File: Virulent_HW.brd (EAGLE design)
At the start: 58.2 x 43 mm, 102 parts, among them SW1 COM08229, SW2 COM08720, SW3 BUTTON, U1 STM32F050G6U6, U2 MAX14536, X1 SMA-142-0711-821/826

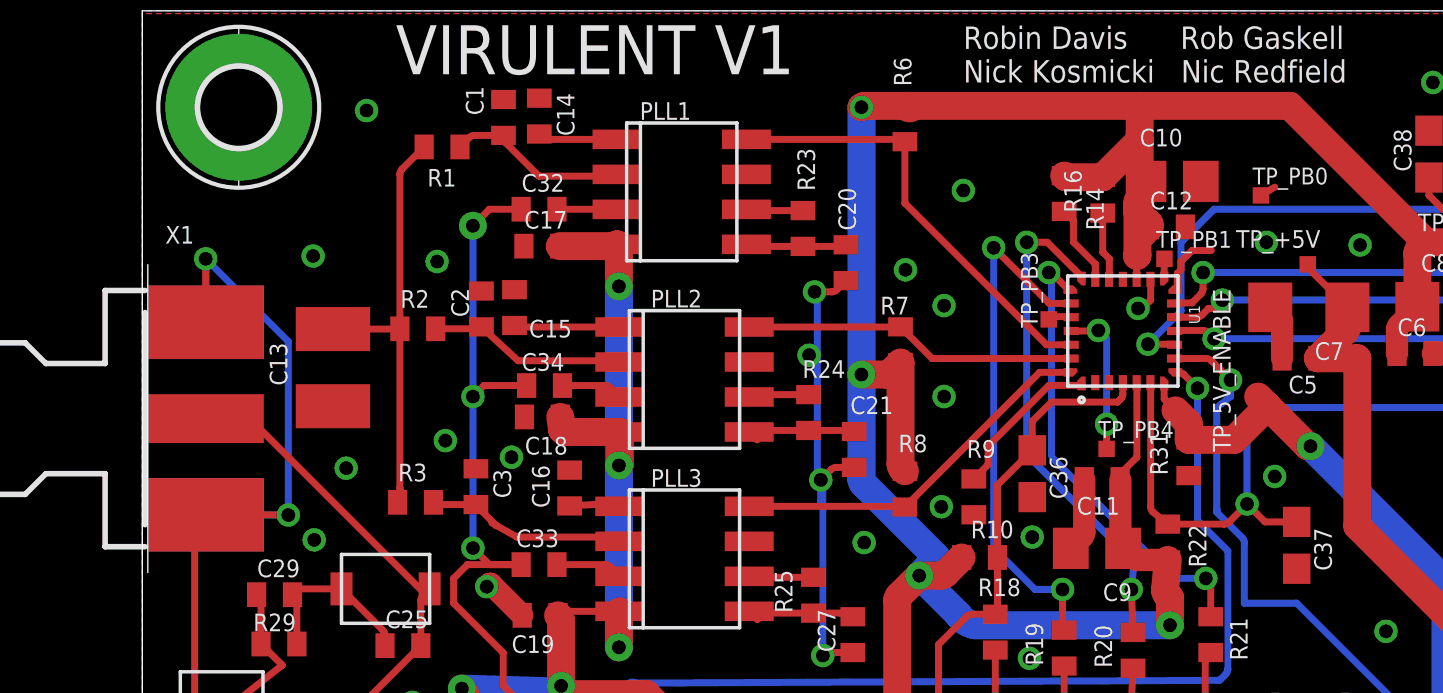
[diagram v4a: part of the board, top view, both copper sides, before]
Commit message: modified silkscreen
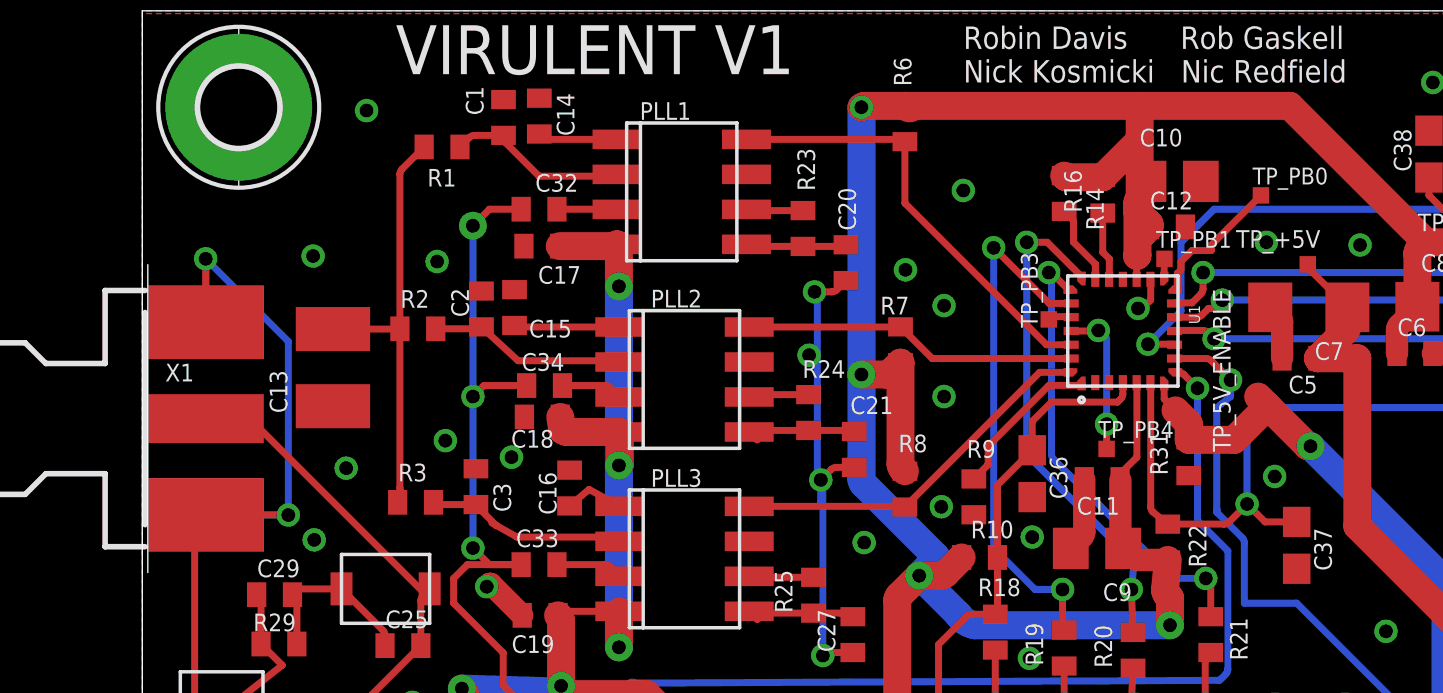
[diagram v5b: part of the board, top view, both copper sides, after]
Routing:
- net PB0: track 2.92 -> 5.09 mm
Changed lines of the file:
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@@
 <setting verticaltext="up"/>
 </settings>
-<grid distance="0.5" unitdist="mm" unit="mm" style="dots" multiple="1" display="no" altdistance="0.05" altunitdist="mm" altunit="mm"/>
+<grid distance="0.5" unitdist="mm" unit="mm" style="dots" multiple="1" display="no" altdistance="0.25" altunitdist="mm" altunit="mm"/>
 <layers>
 <layer number="1" name="Top" color="4" fill="1" visible="yes" active="yes"/>
-<layer number="16" name="Bottom" color="1" fill="1" visible="yes" active="yes"/>
+<layer number="16" name="Bottom" color="1" fill="1" visible="no" active="yes"/>
 <layer number="17" name="Pads" color="2" fill="1" visible="yes" active="yes"/>
 <layer number="18" name="Vias" color="2" fill="1" visible="yes" active="yes"/>
@@
 </element>
 <element name="C3" library="rcl" package="C0402" value="0.1u" x="12.11" y="25.73" smashed="yes" rot="R270">
-<attribute name="NAME" x="12.745" y="26.365" size="0.64" layer="25" rot="R270"/>
+<attribute name="NAME" x="12.745" y="25.865" size="0.64" layer="25" rot="R270"/>
 </element>
 <element name="R3" library="Virulent_HW" package="R0402" value="4.7k" x="9.92" y="25.16" smashed="yes">
@@
 </element>
 <element name="C16" library="rcl" package="C0402" value="2.2u" x="15.51" y="25.68" smashed="yes" rot="R270">
-<attribute name="NAME" x="14.145" y="26.515" size="0.64" layer="25" rot="R270"/>
+<attribute name="NAME" x="14.395" y="26.265" size="0.64" layer="25" rot="R270"/>
 </element>
 <element name="C17" library="rcl" package="C0402" value="1n" x="14.5" y="34.46" smashed="yes">
-<attribute name="NAME" x="13.865" y="35.095" size="0.64" layer="25"/>
+<attribute name="NAME" x="14.365" y="33.095" size="0.64" layer="25"/>
 </element>
 <element name="C18" library="rcl" package="C0402" value="1n" x="14.52" y="28.26" smashed="yes">
-<attribute name="NAME" x="13.885" y="26.895" size="0.64" layer="25"/>
+<attribute name="NAME" x="13.385" y="27.145" size="0.64" layer="25"/>
 </element>
 <element name="C19" library="rcl" package="C0402" value="1n" x="14.44" y="21.06" smashed="yes">
@@
 </element>
 <element name="C13" library="rcl" package="C1210" value="250u" x="6.92" y="30.05" smashed="yes" rot="R270">
-<attribute name="NAME" x="4.625" y="30.955" size="0.64" layer="25" rot="R270"/>
+<attribute name="NAME" x="4.625" y="29.955" size="0.64" layer="25" rot="R270"/>
 </element>
 <element name="R31" library="Virulent_HW" package="R0402" value="10k" x="37.98" y="26.78" smashed="yes" rot="R90">
@@
 </element>
 <element name="C32" library="rcl" package="C0402" value="470n" x="14.4" y="35.8" smashed="yes">
-<attribute name="NAME" x="13.765" y="36.435" size="0.64" layer="25"/>
+<attribute name="NAME" x="14.265" y="36.435" size="0.64" layer="25"/>
 </element>
 <element name="C33" library="rcl" package="C0402" value="470n" x="14.4" y="22.9" smashed="yes">
@@
 <attribute name="MF" value="JOHNSON COMPONENTS" x="0.2" y="28.2" size="1.778" layer="27" display="off"/>
 <attribute name="OC_FARNELL" value="1019328" x="0.2" y="28.2" size="1.778" layer="27" display="off"/>
-<attribute name="NAME" x="0.835" y="34.55" size="0.64" layer="25"/>
+<attribute name="NAME" x="0.835" y="29.55" size="0.64" layer="25"/>
 </element>
 <element name="H1" library="holes" package="2,8-PAD" value="MOUNT-PAD-ROUND2.8" x="54.7" y="3.5"/>
@@
 <wire x1="26.58" y1="3.064790625" x2="26.58" y2="2.04" width="0.254" layer="1"/>
 <wire x1="11.8" y1="15.55" x2="11.679290625" y2="15.5" width="0.16" layer="1" curve="-45"/>
-<wire x1="11.679290625" y1="15.5" x2="10.1" y2="15.5" width="0.16" layer="1"/>
 <via x="4.2" y="16.9" extent="1-16" drill="0.5"/>
 <via x="27.7" y="33.6" extent="1-16" drill="0.5"/>
@@
 <via x="55" y="7.88" extent="1-16" drill="0.5"/>
 <via x="15.6" y="2.6" extent="1-16" drill="0.5"/>
+<wire x1="11.679290625" y1="15.5" x2="10.1" y2="15.5" width="0.16" layer="1"/>
 </signal>
 <signal name="5V_ENABLE">
@@
 <contactref element="C16" pad="2"/>
 <contactref element="PLL3" pad="1"/>
-<wire x1="15.51" y1="25.03" x2="17.2155" y2="25.13" width="0.254" layer="1"/>
-<wire x1="17.2155" y1="25.13" x2="17.3305" y2="25.015" width="0.254" layer="1"/>
+<wire x1="15.51" y1="25.03" x2="16.2155" y2="25.63" width="0.254" layer="1"/>
+<wire x1="16.2155" y1="25.63" x2="17.3305" y2="25.015" width="0.254" layer="1"/>
 </signal>
 <signal name="N$30">
@@
 <wire x1="4.15" y1="21.81" x2="4.31" y2="21.65" width="0.254" layer="1"/>
 <wire x1="4.31" y1="21.65" x2="4.31" y2="20.02" width="0.254" layer="1"/>
+<wire x1="5.08" y1="19.25" x2="2.88" y2="17.51" width="0.254" layer="1"/>
 <wire x1="4.31" y1="20.02" x2="5.08" y2="19.25" width="0.254" layer="1"/>
-<wire x1="5.08" y1="19.25" x2="2.88" y2="17.51" width="0.254" layer="1"/>
 </signal>
 <signal name="PLL_R">
@@
 <wire x1="37.7" y1="33.9" x2="38.1" y2="34.3" width="0.254" layer="1"/>
 <wire x1="38.1" y1="34.3" x2="38.8" y2="34.3" width="0.254" layer="1"/>
-<wire x1="41.1" y1="36.6" x2="40.6" y2="36.3" width="0.254" layer="1"/>
-<wire x1="38.8" y1="34.3" x2="40.6" y2="36.3" width="0" layer="19" extent="1-1"/>
+<wire x1="38.8" y1="34.3" x2="38.8" y2="34.5" width="0.254" layer="1"/>
+<wire x1="38.8" y1="34.5" x2="40.6" y2="36.3" width="0.254" layer="1"/>
 </signal>
 <signal name="PB1">

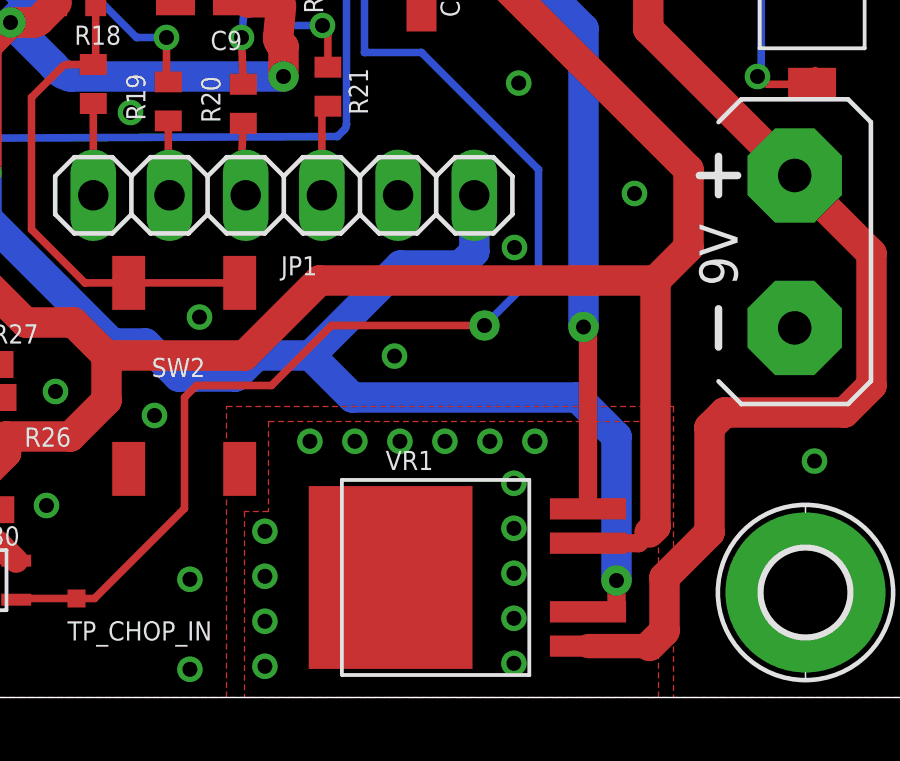
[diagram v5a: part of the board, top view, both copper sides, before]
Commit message: Connected mounting holes to GND.
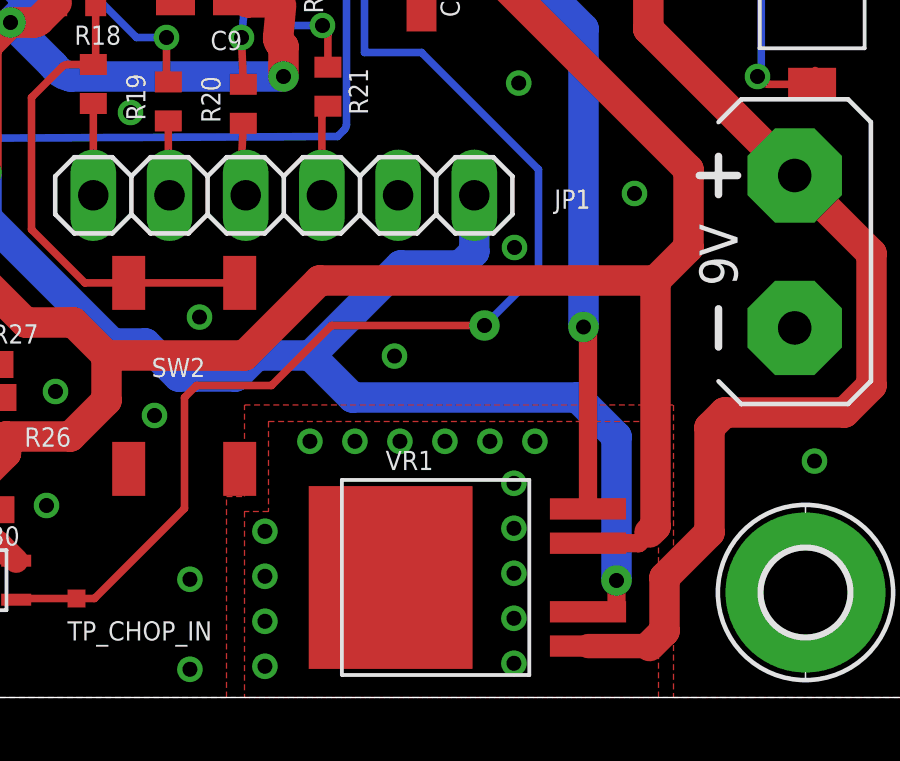
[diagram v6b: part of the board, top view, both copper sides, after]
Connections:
- net GND: now also H1.B2,8, H2.B2,8
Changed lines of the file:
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@@
 <element name="G1" library="battery" package="AB9V" value="AB9V" x="54.34" y="14.86" smashed="yes"/>
 <element name="JP1" library="Virulent_HW" package="1X06" value="" x="37.31" y="16.74" smashed="yes">
-<attribute name="NAME" x="37.2138" y="14.0688" size="0.64" layer="25" ratio="10"/>
+<attribute name="NAME" x="47.5362" y="16.9312" size="0.64" layer="25" ratio="10" rot="R180"/>
 <attribute name="VALUE" x="29.69" y="13.565" size="1.27" layer="27"/>
 </element>
@@
 <vertex x="0" y="0"/>
 <vertex x="35.4" y="0"/>
-<vertex x="35.4" y="9.7"/>
-<vertex x="50.3" y="9.7"/>
+<vertex x="35.4" y="6.7"/>
+<vertex x="36" y="6.7"/>
+<vertex x="36" y="9.75"/>
+<vertex x="50.3" y="9.75"/>
 <vertex x="50.3" y="0"/>
 <vertex x="58.2" y="0"/>
@@
 <via x="15.6" y="2.6" extent="1-16" drill="0.5"/>
 <wire x1="11.679290625" y1="15.5" x2="10.1" y2="15.5" width="0.16" layer="1"/>
+<contactref element="H1" pad="B2,8"/>
+<contactref element="H2" pad="B2,8"/>
 </signal>
 <signal name="5V_ENABLE">
